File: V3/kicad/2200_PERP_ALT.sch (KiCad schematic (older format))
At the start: 2 parts, among them J2200 Conn_01x08_Male, U2200 65C22QFP

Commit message: Updated PCB files
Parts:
- removed U2200: 65C22QFP, Package_QFP:LQFP-44_10x10mm_P0.8mm, symbol 65C22PLCC:65C22QFP
- added C2200: 22pf, Capacitor_THT:C_Rect_L4.0mm_W2.5mm_P2.50mm, symbol Device:C
- added J2201: Conn_01x08_Male, Connector_PinHeader_2.54mm:PinHeader_1x08_P2.54mm_Vertical, symbol Connector:Conn_01x08_Male
- added RN2200, RN2201: 10k, Resistor_THT:R_Array_SIP9, symbol Device:R_Network08
- added U2200: PIO-LQFP-44, Package_QFP:LQFP-44_10x10mm_P0.8mm, symbol Zilog_Z80_Peripherals:PIO-LQFP-44
- J2200: footprint (none) -> Connector_PinHeader_2.54mm:PinHeader_1x08_P2.54mm_Vertical
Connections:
- net +5V: now also C2200.1, RN2200.1 (common), RN2201.1 (common), U2200.32 (IEI), U2200.34 (VCC)
- net CLK: now also U2200.33 (CLK)
- net CS: now also U2200.10 (~CE~)
- net CS0: now also RN2200.4 (R3), U2200.20 (PA2)
- net CS1: now also RN2200.5 (R4), U2200.19 (PA3)
- net CS2: now also RN2200.6 (R5), U2200.16 (PA4)
- net CS3: now also RN2200.7 (R6), U2200.15 (PA5)
- net CS4: now also RN2200.8 (R7), U2200.14 (PA6)
- net GND: now also C2200.2, U2200.18 (GND)
- net MISO: now also J2200.1 (Pin_1), RN2200.2 (R1), U2200.22 (PA0); no longer J2200.3 (Pin_3)
- net MOSI: now also J2200.3 (Pin_3), RN2200.9 (R8), U2200.13 (PA7); no longer J2200.1 (Pin_1)
- net SCK: now also RN2200.3 (R2), U2200.21 (PA1)
- new net: J2201.8 (Pin_8), RN2201.9 (R8), U2200.35 (PB0)
- new net: J2201.7 (Pin_7), RN2201.8 (R7), U2200.36 (PB1)
- new net: J2201.6 (Pin_6), RN2201.7 (R6), U2200.37 (PB2)
- new net: J2201.5 (Pin_5), RN2201.6 (R5), U2200.38 (PB3)
- new net: J2201.4 (Pin_4), RN2201.5 (R4), U2200.40 (PB4)
- new net: J2201.3 (Pin_3), RN2201.4 (R3), U2200.41 (PB5)
- new net: J2201.2 (Pin_2), RN2201.3 (R2), U2200.42 (PB6)
- new net: J2201.1 (Pin_1), RN2201.2 (R1), U2200.43 (PB7)
- new net A0: U2200.12 (B/~A~)
- new net A1: U2200.11 (C/~D~)
- new net D0: U2200.26 (D0)
- new net D1: U2200.27 (D1)
- new net D2: U2200.7 (D2)
- new net D3: U2200.6 (D3)
- new net D4: U2200.5 (D4)
- new net D5: U2200.4 (D5)
- new net D6: U2200.9 (D6)
- new net D7: U2200.8 (D7)
- new net INT: U2200.31 (~INT~)
- new net IORQ: U2200.1 (~IORQ~)
- new net M1: U2200.3 (~M1~)
- new net RD: U2200.44 (~RD~)
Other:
- note added: "MSB first"
- note added: "This page has been checked!"

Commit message: last touches on peripherals and memory
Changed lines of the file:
@@
 P 3350 5150
 F 0 "#PWR0111" H 3350 4900 50  0001 C CNN
-F 1 "GND" V 3355 5022 50  0000 R CNN
+F 1 "GND" H 3600 5150 50  0000 R CNN
 F 2 "" H 3350 5150 50  0001 C CNN
 F 3 "" H 3350 5150 50  0001 C CNN
@@
 Text Notes 6100 3250 0    50   ~ 0
 MSB first
-Text HLabel 2500 4650 0    50   Output ~ 0
+Text HLabel 2850 4650 0    50   Output ~ 0
 INT
 Text Label 2700 2750 0    50   ~ 0
@@
 U 1 1 62184408
 P 5000 5100
-F 0 "RN2201" V 4383 5100 50  0000 C CNN
-F 1 "10k" V 4474 5100 50  0000 C CNN
+F 0 "RN2201" H 4350 5000 50  0000 C CNN
+F 1 "10k" H 4400 5100 50  0000 C CNN
 F 2 "Resistor_THT:R_Array_SIP9" V 5475 5100 50  0001 C CNN
 F 3 "http://www.vishay.com/docs/31509/csc.pdf" H 5000 5100 50  0001 C CNN
@@
 	-1   0    0    1
 $EndComp
-Wire Wire Line
-	2850 4650 2500 4650
-Text Label 2700 4650 2    50   ~ 0
-INT
 $Sheet
 S 7600 2850 600  600

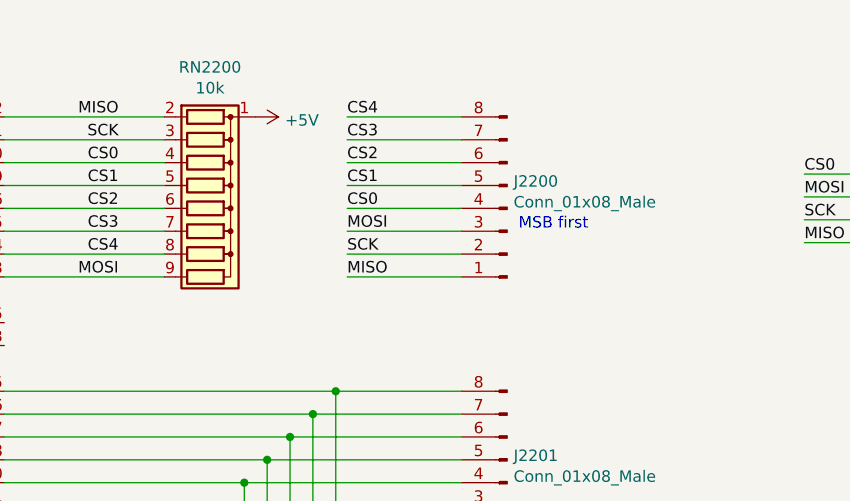
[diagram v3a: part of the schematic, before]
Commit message: fixed up PIO routing
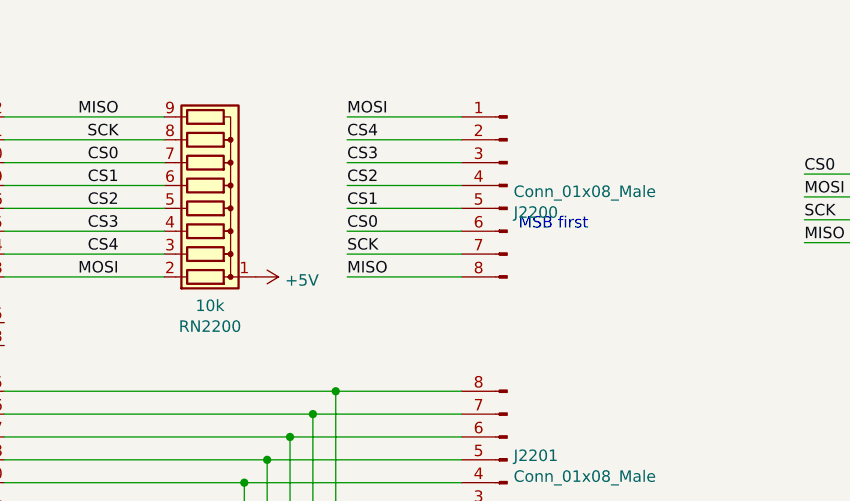
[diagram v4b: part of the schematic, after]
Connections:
- net CS0: now also J2200.6 (Pin_6), RN2200.7 (R6); no longer J2200.4 (Pin_4), RN2200.4 (R3)
- net CS1: now also RN2200.6 (R5); no longer RN2200.5 (R4)
- net CS2: now also J2200.4 (Pin_4), RN2200.5 (R4); no longer J2200.6 (Pin_6), RN2200.6 (R5)
- net CS3: now also J2200.3 (Pin_3), RN2200.4 (R3); no longer J2200.7 (Pin_7), RN2200.7 (R6)
- net CS4: now also J2200.2 (Pin_2), RN2200.3 (R2); no longer J2200.8 (Pin_8), RN2200.8 (R7)
- net MISO: now also J2200.8 (Pin_8), RN2200.9 (R8); no longer J2200.1 (Pin_1), RN2200.2 (R1)
- net MOSI: now also J2200.1 (Pin_1), RN2200.2 (R1); no longer J2200.3 (Pin_3), RN2200.9 (R8)
- net SCK: now also J2200.7 (Pin_7), RN2200.8 (R7); no longer J2200.2 (Pin_2), RN2200.3 (R2)
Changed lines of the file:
@@
 L Connector:Conn_01x08_Male J2200
 U 1 1 6207A119
-P 6050 3150
-F 0 "J2200" H 6022 3032 50  0000 R CNN
-F 1 "Conn_01x08_Male" H 6022 3123 50  0000 R CNN
-F 2 "Connector_PinHeader_2.54mm:PinHeader_1x08_P2.54mm_Vertical" H 6050 3150 50  0001 C CNN
-F 3 "~" H 6050 3150 50  0001 C CNN
-	1    6050 3150
-	-1   0    0    1
+P 6050 3050
+F 0 "J2200" H 6022 2932 50  0000 R CNN
+F 1 "Conn_01x08_Male" H 6022 3023 50  0000 R CNN
+F 2 "Connector_PinHeader_2.54mm:PinHeader_1x08_P2.54mm_Vertical" H 6050 3050 50  0001 C CNN
+F 3 "~" H 6050 3050 50  0001 C CNN
+	1    6050 3050
+	-1   0    0    -1
 $EndComp
 Text HLabel 2850 4250 0    50   Input ~ 0
@@
 Wire Wire Line
 	5350 3450 5850 3450
-Text Label 5350 3250 0    50   ~ 0
+Text Label 5350 2750 0    50   ~ 0
 MOSI
 Wire Wire Line
@@
 Wire Wire Line
 	5850 2750 5350 2750
+Text Label 5350 3250 0    50   ~ 0
+CS0
 Text Label 5350 3150 0    50   ~ 0
-CS0
+CS1
+Text Label 5350 2950 0    50   ~ 0
+CS3
 Text Label 5350 3050 0    50   ~ 0
-CS1
+CS2
 Text Label 5350 2850 0    50   ~ 0
-CS3
-Text Label 5350 2950 0    50   ~ 0
-CS2
-Text Label 5350 2750 0    50   ~ 0
 CS4
 Text Label 4350 3050 2    50   ~ 0
@@
 L Device:R_Network08 RN2200
 U 1 1 6213A6F8
-P 4750 3150
-F 0 "RN2200" V 4133 3150 50  0000 C CNN
-F 1 "10k" V 4224 3150 50  0000 C CNN
-F 2 "Resistor_THT:R_Array_SIP9" V 5225 3150 50  0001 C CNN
-F 3 "http://www.vishay.com/docs/31509/csc.pdf" H 4750 3150 50  0001 C CNN
-	1    4750 3150
-	0    1    1    0
+P 4750 3050
+F 0 "RN2200" V 4133 3050 50  0000 C CNN
+F 1 "10k" V 4224 3050 50  0000 C CNN
+F 2 "Resistor_THT:R_Array_SIP9" V 5225 3050 50  0001 C CNN
+F 3 "http://www.vishay.com/docs/31509/csc.pdf" H 4750 3050 50  0001 C CNN
+	1    4750 3050
+	0    1    -1   0
 $EndComp
 Wire Wire Line
@@
 L power:+5V #PWR0128
 U 1 1 621809FF
-P 4950 2750
-F 0 "#PWR0128" H 4950 2600 50  0001 C CNN
-F 1 "+5V" V 4965 2878 50  0000 L CNN
-F 2 "" H 4950 2750 50  0001 C CNN
-F 3 "" H 4950 2750 50  0001 C CNN
-	1    4950 2750
+P 4950 3450
+F 0 "#PWR0128" H 4950 3300 50  0001 C CNN
+F 1 "+5V" V 4965 3578 50  0000 L CNN
+F 2 "" H 4950 3450 50  0001 C CNN
+F 3 "" H 4950 3450 50  0001 C CNN
+	1    4950 3450
 	0    1    1    0
 $EndComp

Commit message: Design Rule Check
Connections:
- no-connect marks 1 -> 5
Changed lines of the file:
@@
 	1    0    0    -1
 $EndComp
+NoConn ~ 3850 4850
+NoConn ~ 3850 4950
+NoConn ~ 3850 3650
+NoConn ~ 3850 3750
 Wire Bus Line
 	2600 2650 2600 3350

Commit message: just totally redid the whole thing
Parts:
- removed RN2201: 10k, Resistor_THT:R_Array_SIP9, symbol Device:R_Network08
- C2200: footprint Capacitor_THT:C_Rect_L4.0mm_W2.5mm_P2.50mm -> Capacitor_SMD:C_1206_3216Metric
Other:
- moved on the sheet: J2201
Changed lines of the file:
@@
 $Descr A4 11693 8268
 encoding utf-8
-Sheet 4 9
+Sheet 4 8
 Title ""
 Date ""
@@
 	0    1    1    0
 $EndComp
-$Comp
-L Device:R_Network08 RN2201
-U 1 1 62184408
-P 5000 5100
-F 0 "RN2201" H 4350 5000 50  0000 C CNN
-F 1 "10k" H 4400 5100 50  0000 C CNN
-F 2 "Resistor_THT:R_Array_SIP9" V 5475 5100 50  0001 C CNN
-F 3 "http://www.vishay.com/docs/31509/csc.pdf" H 5000 5100 50  0001 C CNN
-	1    5000 5100
-	1    0    0    1
-$EndComp
-$Comp
-L power:+5V #PWR0129
-U 1 1 62184416
-P 4600 5300
-F 0 "#PWR0129" H 4600 5150 50  0001 C CNN
-F 1 "+5V" V 4615 5428 50  0000 L CNN
-F 2 "" H 4600 5300 50  0001 C CNN
-F 3 "" H 4600 5300 50  0001 C CNN
-	1    4600 5300
-	-1   0    0    1
-$EndComp
 $Sheet
 S 7600 2850 600  600
@@
 Wire Wire Line
 	7350 3000 7600 3000
-$Sheet
-S 8850 2850 550  600
-U 62602013
-F0 "2220_ROM" 50
-F1 "2220_ROM.sch" 50
-F2 "CS" I L 8850 3000 50
-F3 "MOSI" I L 8850 3100 50
-F4 "MISO" O L 8850 3300 50
-F5 "SCK" I L 8850 3200 50
-$EndSheet
 Text Notes 7850 6950 0    118  ~ 24
 This page has been checked!
-Wire Wire Line
-	8850 3100 8600 3100
-Wire Wire Line
-	8850 3200 8600 3200
-Text Label 8600 3100 0    50   ~ 0
-MOSI
-Text Label 8600 3200 0    50   ~ 0
-SCK
-Text Label 8600 3300 0    50   ~ 0
-MISO
-Wire Wire Line
-	8850 3300 8600 3300
-Text Label 8600 3000 0    50   ~ 0
-CS1
-Wire Wire Line
-	8600 3000 8850 3000
 $Comp
 L Connector:Conn_01x08_Male J2201
 U 1 1 6261A38A
-P 6050 4350
-F 0 "J2201" H 6022 4232 50  0000 R CNN
-F 1 "Conn_01x08_Male" H 6022 4323 50  0000 R CNN
-F 2 "Connector_PinHeader_2.54mm:PinHeader_1x08_P2.54mm_Vertical" H 6050 4350 50  0001 C CNN
-F 3 "~" H 6050 4350 50  0001 C CNN
-	1    6050 4350
+P 4050 4350
+F 0 "J2201" H 4022 4232 50  0000 R CNN
+F 1 "Conn_01x08_Male" H 4022 4323 50  0000 R CNN
+F 2 "Connector_PinHeader_2.54mm:PinHeader_1x08_P2.54mm_Vertical" H 4050 4350 50  0001 C CNN
+F 3 "~" H 4050 4350 50  0001 C CNN
+	1    4050 4350
 	-1   0    0    1
 $EndComp
-Wire Wire Line
-	3850 4650 4600 4650
-Wire Wire Line
-	4600 4900 4600 4650
-Connection ~ 4600 4650
-Wire Wire Line
-	4600 4650 5850 4650
-Wire Wire Line
-	3850 4550 4700 4550
-Wire Wire Line
-	3850 4450 4800 4450
-Wire Wire Line
-	4700 4900 4700 4550
-Connection ~ 4700 4550
-Wire Wire Line
-	4700 4550 5850 4550
-Wire Wire Line
-	4800 4900 4800 4450
-Connection ~ 4800 4450
-Wire Wire Line
-	4800 4450 5850 4450
-Wire Wire Line
-	3850 4350 4900 4350
-Wire Wire Line
-	3850 4250 5000 4250
-Wire Wire Line
-	3850 4150 5100 4150
-Wire Wire Line
-	3850 4050 5200 4050
-Wire Wire Line
-	3850 3950 5300 3950
-Wire Wire Line
-	4900 4900 4900 4350
-Connection ~ 4900 4350
-Wire Wire Line
-	5100 4900 5100 4150
-Connection ~ 5100 4150
-Wire Wire Line
-	5100 4150 5850 4150
-Connection ~ 5000 4250
-Wire Wire Line
-	5000 4250 5850 4250
-Wire Wire Line
-	5000 4250 5000 4900
-Wire Wire Line
-	4900 4350 5850 4350
-Wire Wire Line
-	5200 4900 5200 4050
-Connection ~ 5200 4050
-Wire Wire Line
-	5200 4050 5850 4050
-Wire Wire Line
-	5300 4900 5300 3950
-Connection ~ 5300 3950
-Wire Wire Line
-	5300 3950 5850 3950
 $Comp
 L Device:C C?
@@
 F 0 "C2200" H 1365 3046 50  0000 L CNN
 F 1 "22pf" H 1365 2955 50  0000 L CNN
-F 2 "Capacitor_THT:C_Rect_L4.0mm_W2.5mm_P2.50mm" H 1288 2850 50  0001 C CNN
+F 2 "Capacitor_SMD:C_1206_3216Metric" H 1288 2850 50  0001 C CNN
 F 3 "~" H 1250 3000 50  0001 C CNN
 	1    1250 3000

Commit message: More rearranging
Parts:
- added J2202: Conn_01x02_Male, Connector_PinHeader_2.54mm:PinHeader_1x02_P2.54mm_Vertical, symbol Connector:Conn_01x02_Male
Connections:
- net +5V: now also J2202.1 (Pin_1)
- net GND: now also J2202.2 (Pin_2)
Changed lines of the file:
@@
 	1    0    0    -1
 $EndComp
-Text Notes 6100 3250 0    50   ~ 0
+Text Notes 6100 3300 0    50   ~ 0
 MSB first
 Text HLabel 2850 4650 0    50   Output ~ 0
@@
 NoConn ~ 3850 3650
 NoConn ~ 3850 3750
+$Comp
+L Connector:Conn_01x02_Male J2202
+U 1 1 62EBE199
+P 6050 3750
+F 0 "J2202" H 6022 3632 50  0000 R CNN
+F 1 "Conn_01x02_Male" H 6022 3723 50  0000 R CNN
+F 2 "Connector_PinHeader_2.54mm:PinHeader_1x02_P2.54mm_Vertical" H 6050 3750 50  0001 C CNN
+F 3 "~" H 6050 3750 50  0001 C CNN
+	1    6050 3750
+	-1   0    0    1
+$EndComp
+$Comp
+L power:+5V #PWR0159
+U 1 1 62EBEF84
+P 5850 3750
+F 0 "#PWR0159" H 5850 3600 50  0001 C CNN
+F 1 "+5V" V 5865 3878 50  0000 L CNN
+F 2 "" H 5850 3750 50  0001 C CNN
+F 3 "" H 5850 3750 50  0001 C CNN
+	1    5850 3750
+	0    -1   -1   0
+$EndComp
+$Comp
+L power:GND #PWR0163
+U 1 1 62EBFB90
+P 5850 3650
+F 0 "#PWR0163" H 5850 3400 50  0001 C CNN
+F 1 "GND" H 5850 3350 50  0001 R CNN
+F 2 "" H 5850 3650 50  0001 C CNN
+F 3 "" H 5850 3650 50  0001 C CNN
+	1    5850 3650
+	0    1    1    0
+$EndComp
 Wire Bus Line
 	2600 2650 2600 3350
